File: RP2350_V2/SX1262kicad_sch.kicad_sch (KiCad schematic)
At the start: 29 parts

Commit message: Transceiver components and schematic final?
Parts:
- removed L10: 0R, rlc_402_smd, symbol reference-altium-import:root_0_Inductor
- C1: renamed from C44; footprint rlc_402_smd -> Capacitor_SMD:C_0402_1005Metric; LCSC (none) -> C47339
- C10: renamed from C57; footprint rlc_402_smd -> Capacitor_SMD:C_0402_1005Metric; LCSC (none) -> C86288
- C11: renamed from C58; footprint rlc_402_smd -> Capacitor_SMD:C_0402_1005Metric; LCSC (none) -> C1553
- C12: renamed from C60; value Cap -> 1n; footprint rlc_402_smd -> Capacitor_SMD:C_0402_1005Metric; LCSC (none) -> C14442
- C13: renamed from C59; footprint rlc_402_smd -> Capacitor_SMD:C_0402_1005Metric; LCSC (none) -> C14442
- C14: renamed from C61; footprint rlc_402_smd -> Capacitor_SMD:C_0402_1005Metric
- C15: renamed from C62; footprint rlc_402_smd -> Capacitor_SMD:C_0402_1005Metric; LCSC (none) -> C307447
- C16: renamed from C63; footprint rlc_402_smd -> Capacitor_SMD:C_0402_1005Metric; LCSC (none) -> C307447
- C2: renamed from C47; footprint rlc_402_smd -> Capacitor_SMD:C_0402_1005Metric; LCSC (none) -> C1525
- C3: renamed from C48; footprint rlc_402_smd -> Capacitor_SMD:C_0402_1005Metric; LCSC (none) -> C14445
- C4: renamed from C49; footprint rlc_402_smd -> Capacitor_SMD:C_0402_1005Metric; LCSC (none) -> C307339
- C5: renamed from C50; footprint rlc_402_smd -> Capacitor_SMD:C_0402_1005Metric; LCSC (none) -> C84706
- C6: renamed from C52; footprint rlc_402_smd -> Capacitor_SMD:C_0402_1005Metric; LCSC (none) -> C1553
- C7: renamed from C53; footprint rlc_402_smd -> Capacitor_SMD:C_0402_1005Metric; LCSC (none) -> C318583
- C8: renamed from C54; footprint rlc_402_smd -> Capacitor_SMD:C_0402_1005Metric; LCSC (none) -> C318575
- C9: renamed from C55; footprint rlc_402_smd -> Capacitor_SMD:C_0402_1005Metric; LCSC (none) -> C318570
- L1: renamed from L9; footprint rlc_805_smd enlarged -> Inductor_SMD:L_0805_2012Metric; LCSC (none) -> C75634
- L3: renamed from L11; footprint rlc_402_smd -> Inductor_SMD:L_0402_1005Metric; LCSC (none) -> C27151
- L4: renamed from L12; footprint rlc_402_smd -> Inductor_SMD:L_0402_1005Metric; LCSC (none) -> C76787
- L5: renamed from L13; footprint rlc_402_smd -> Inductor_SMD:L_0402_1005Metric; LCSC (none) -> C778764
- L6: renamed from L14; footprint rlc_402_smd -> Inductor_SMD:L_0402_1005Metric; LCSC (none) -> C13595
- L7: renamed from L15; footprint rlc_402_smd -> Inductor_SMD:L_0402_1005Metric; LCSC (none) -> C74297
- R1: renamed from R36; value Resistor -> 100; footprint rlc_402_smd -> Resistor_SMD:R_0402_1005Metric; LCSC (none) -> C25076
- R2: renamed from R35; footprint rlc_402_smd -> Resistor_SMD:R_0402_1005Metric; LCSC (none) -> C25076
- RFIO1: footprint SMA_end_launch_1.0mm_9.52mm -> My_Footprints:RF_CONN_LINX_CONSMA002-SMD-G-T; LCSC (none) -> C22372912
- U1: renamed from U7; footprint (none) -> My_Footprints:SX1262_QFN24_4X4_SEM; LCSC (none) -> C191341
- U2: renamed from U8; footprint (none) -> My_Footprints:PE4259_RF_SW; LCSC (none) -> C470892
- XTAL1: footprint NX2016SA_NDK -> My_Footprints:NX2016SA_NDK; LCSC (none) -> C1986260
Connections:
- net GND: now also U1.25 (GND)
- net at U1.23 (RFO): now also C7.2, L3.1, L5.1
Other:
- note removed: "for consistency, can we replace all the ground symbols here with this one"

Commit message: updates
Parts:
- removed RFIO1: SMA, My_Footprints:RF_CONN_LINX_CONSMA002-SMD-G-T, symbol reference-altium-import:root_0_mirrored_SMA
- added J2: 901-143-6RFX, My_Footprints:RF_ANT_OUTPUT_901-143-6RFX, symbol My_Library:901-143-6RFX
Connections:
- net GND: now also J2.2 (GND), J2.3 (GND), J2.4 (GND), J2.5 (GND)
- net at C16.2, L7.2: now also J2.1
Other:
- moved on the sheet: C16

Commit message: initial Transceiver layout
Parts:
- J2: LCSC (none) -> C429844
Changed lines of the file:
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@@
+			)
+		)
+		(property "LCSC" "C429844"
+			(at 276.86 78.74 0)
+			(effects
+				(font
+					(size 1.27 1.27)
+				)
+				(hide yes)
 			)
 		)

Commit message: progress :D
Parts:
- removed J2: 901-143-6RFX, My_Footprints:RF_ANT_OUTPUT_901-143-6RFX, symbol My_Library:901-143-6RFX
- added J4: RF_CONNECTOR_5-1814832-2, My_Footprints:RF_CONNECTOR_518148322, symbol My_Library:RF_CONNECTOR_5-1814832-2
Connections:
- net GND: now also J4.2, J4.3, J4.4, J4.5
- net at C16.2, L7.2: now also J4.1
- net BUSY renamed uC_BUSY
- net MISO renamed SPIO_RX
- net MOSI renamed SPI0_TX
- net NSS renamed CS/NSS
- net SCK renamed SPIO_CLK
- net SX_NRESET renamed uC_RESET
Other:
- moved on the sheet: C14, C15, C16, C6, C8, L4, L7, U2

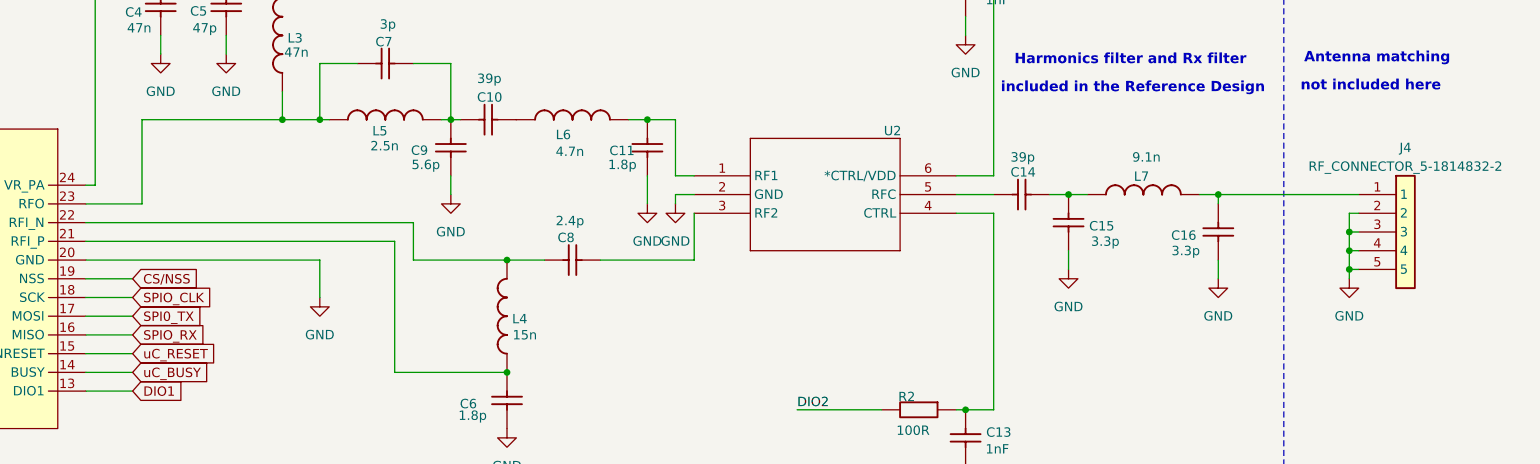
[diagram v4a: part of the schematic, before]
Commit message: fixed RF impedance matched width, changed rf connector, etc.
DRC+DFM clean with waivers. Pending final review for tapeout.
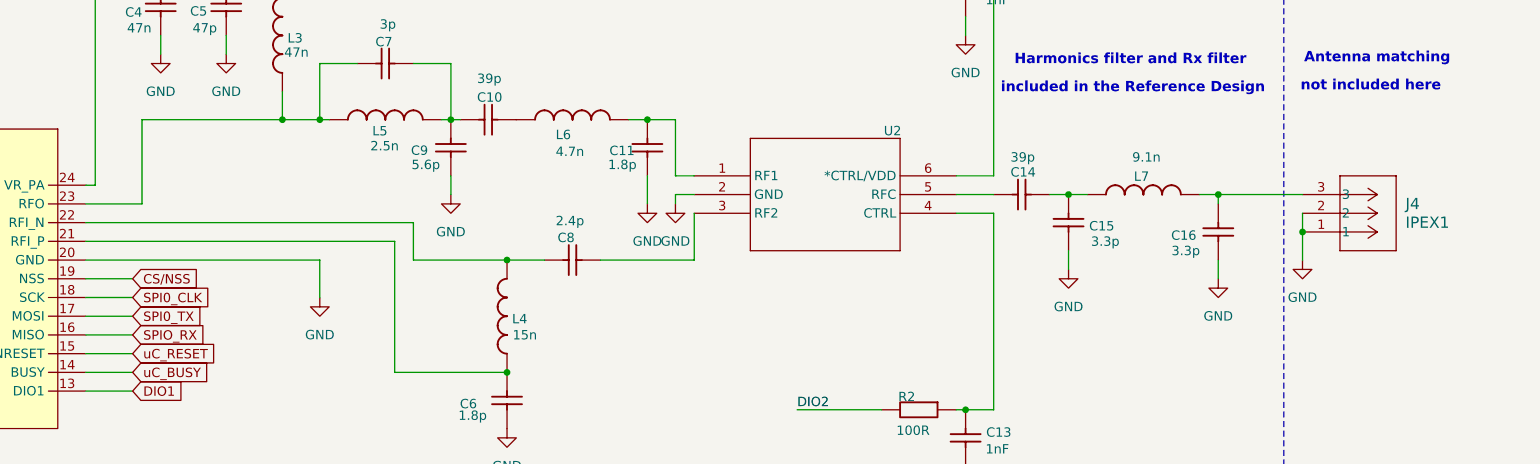
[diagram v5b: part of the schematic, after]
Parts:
- removed J4: RF_CONNECTOR_5-1814832-2, My_Footprints:RF_CONNECTOR_518148322, symbol My_Library:RF_CONNECTOR_5-1814832-2
- added J4: IPEX1, My_Footprints:MHF I_RECE_IPX, symbol My_Library:IPEX1
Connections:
- net GND: now also J4.1, J4.2
- net at C16.2, L7.2: now also J4.3
- net SPIO_CLK renamed SPI0_CLK
